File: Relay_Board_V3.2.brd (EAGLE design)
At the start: 140 x 100 mm, 59 parts

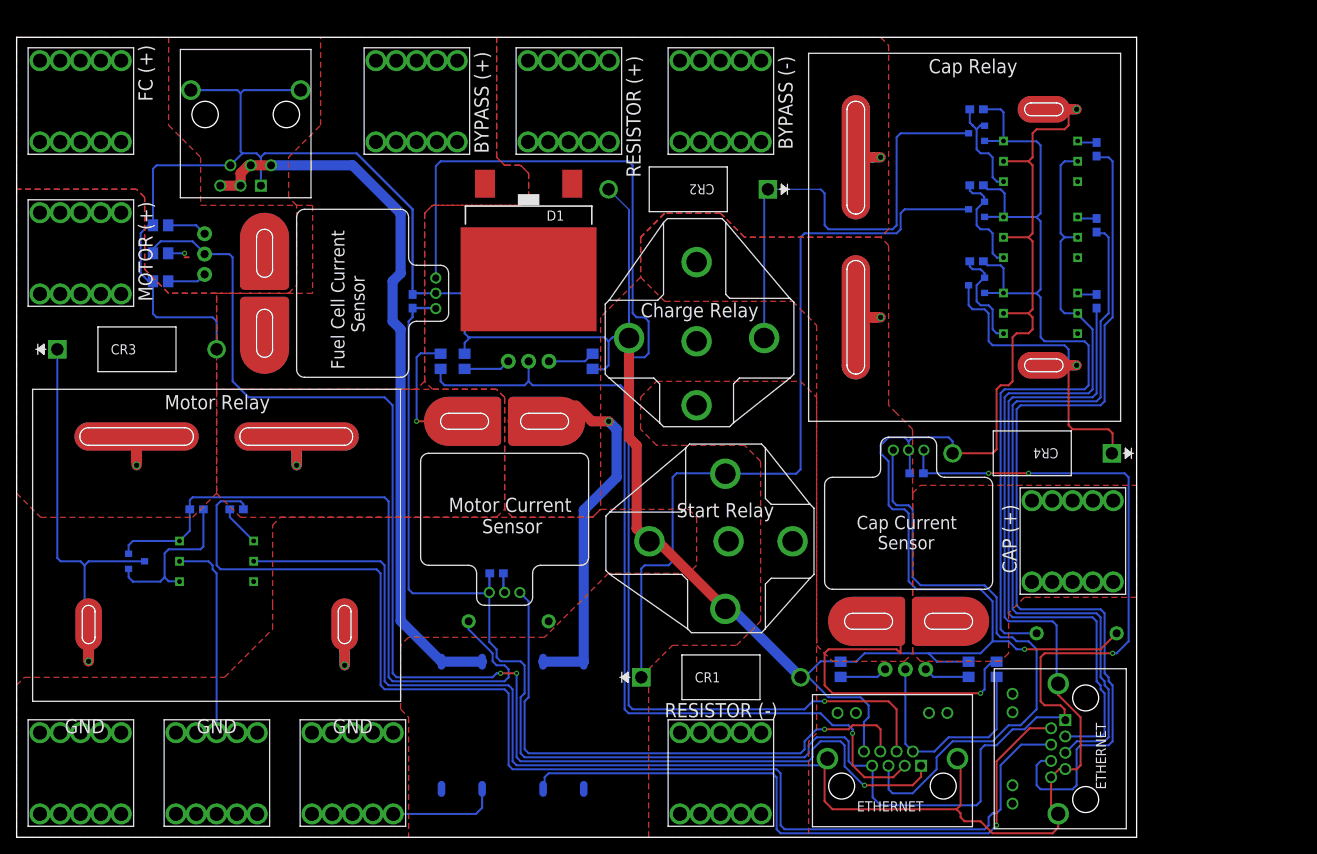
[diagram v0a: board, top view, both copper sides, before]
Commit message: Added RJ-11
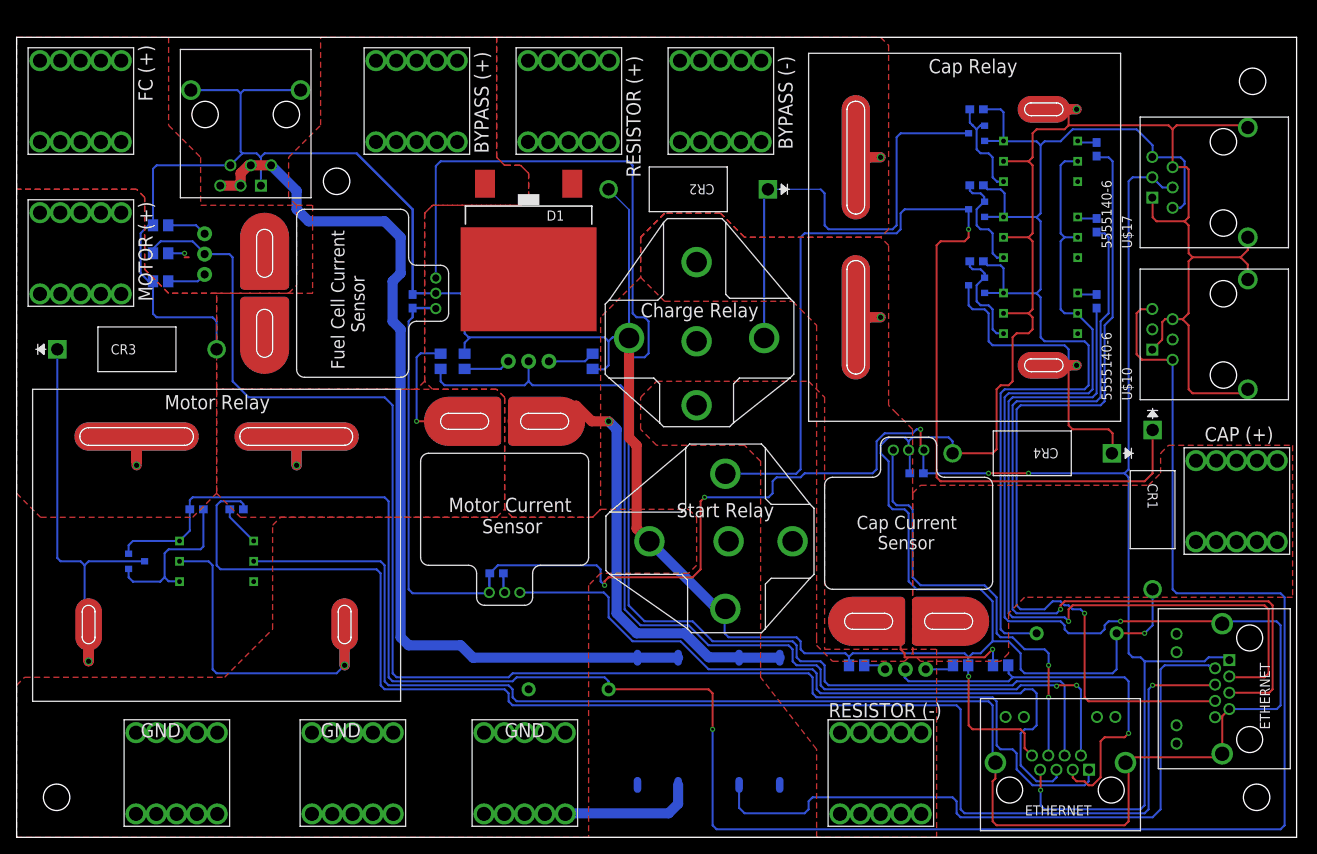
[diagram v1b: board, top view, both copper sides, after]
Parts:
- added U$10, U$17: 5555140-6, 5555140-6 RJ11:1734723-1_RJ11
- added U$18, U$20, U$21, U$23: (no value), SparkFun-Electromechanical:STAND-OFF
- moved CR1 45.4 mm to (142.0, 31.0), turned to 270 degrees
- moved U$22 24.5 mm to (86.5, 14.5)
- moved FCC_1 21.8 mm to (154.1, 18.6)
- moved FC.GND 21.5 mm to (63.5, 8.00)
- moved CAP.POS 21.1 mm to (152.5, 42.0)
- moved FCC_2 21.0 mm to (130.5, 5.90)
- moved RES.NEG 20.0 mm to (108.0, 8.00)
- moved MOTOR.GROUND 17.0 mm to (42.0, 8.00)
- moved CAP.GND 12.0 mm to (20.0, 8.00)
- moved U$16 11.3 mm to (69.0, 18.5), turned to 0 degrees
- moved R4 2.06 mm to (105.0, 21.5), turned to 0 degrees
- moved R14 1.12 mm to (118.0, 21.5), turned to 180 degrees
- moved R5 0.71 mm to (123.0, 21.5), turned to 180 degrees
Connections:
- net 5V: now also U$17.2, U$17.5
- net AUX.12: now also U$10.3, U$10.4
- net CAP_CURR: now also FCC_2.P$6; no longer FCC_2.P$5
- net CAP_VOLT: now also FCC_2.P$3; no longer FCC_2.P$2
- net FC.12: now also U$17.3, U$17.4
- net GND: now also U$10.1, U$10.6, U$10.SH1, U$10.SH2, U$17.1, U$17.6, U$17.SH1, U$17.SH2
- net MOTOR_CURR: now also FCC_2.P$5; no longer FCC_2.P$6
- net MOTOR_VOLT: now also FCC_2.P$2; no longer FCC_2.P$3
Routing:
- net AUX.12: track 85.6 -> 274.9 mm, vias 0 -> 1
- net GND: track 447.1 -> 579.1 mm, vias 3 -> 4
- net ISO_GND: track 250.9 -> 295.5 mm, vias 0 -> 1
- net 5V: track 231.8 -> 269.2 mm, vias 3 -> 6
- net N$30: track 97.6 -> 132.3 mm, vias 0 -> 1
- net FC.12: track 120.5 -> 149.0 mm
- net CAP_SENSOR: track 47.0 -> 21.1 mm
- net MOTOR_R: track 155.3 -> 181.1 mm, vias 0 -> 1
- net POWER_BOARD: track 91.1 -> 116.2 mm
- net CAP_VOLT: track 28.8 -> 51.6 mm, vias 0 -> 1
- net CAP_CURR: track 74.1 -> 54.2 mm, vias 0 -> 2
- net MOTOR_CURR: track 70.0 -> 89.8 mm, vias 1 -> 0
- net MOTOR_VOLT: track 109.7 -> 127.4 mm, vias 1 -> 2
- net FC_CURR: track 149.7 -> 167.3 mm, vias 1 -> 0
- net CAP_R: track 79.5 -> 96.6 mm, vias 0 -> 1
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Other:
- board size 140 x 100 mm -> 160 x 100 mm
